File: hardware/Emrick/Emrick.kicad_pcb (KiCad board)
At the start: 4 copper layers, 44.4 x 59.2 mm, 90 parts, among them J1 LED_STRIP_CONNECTOR, J3 Conn_02x05_Odd_Even, J4 BATT_CONN, P1 USB_C_Plug_USB2.0, Q1 Q_NMOS_GSD, Q2 Q_NMOS_GSD, Q3 Q_NMOS_GSD, SW1 SW_SPST, SW2 SW_Push_LED, U1 74HCT541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

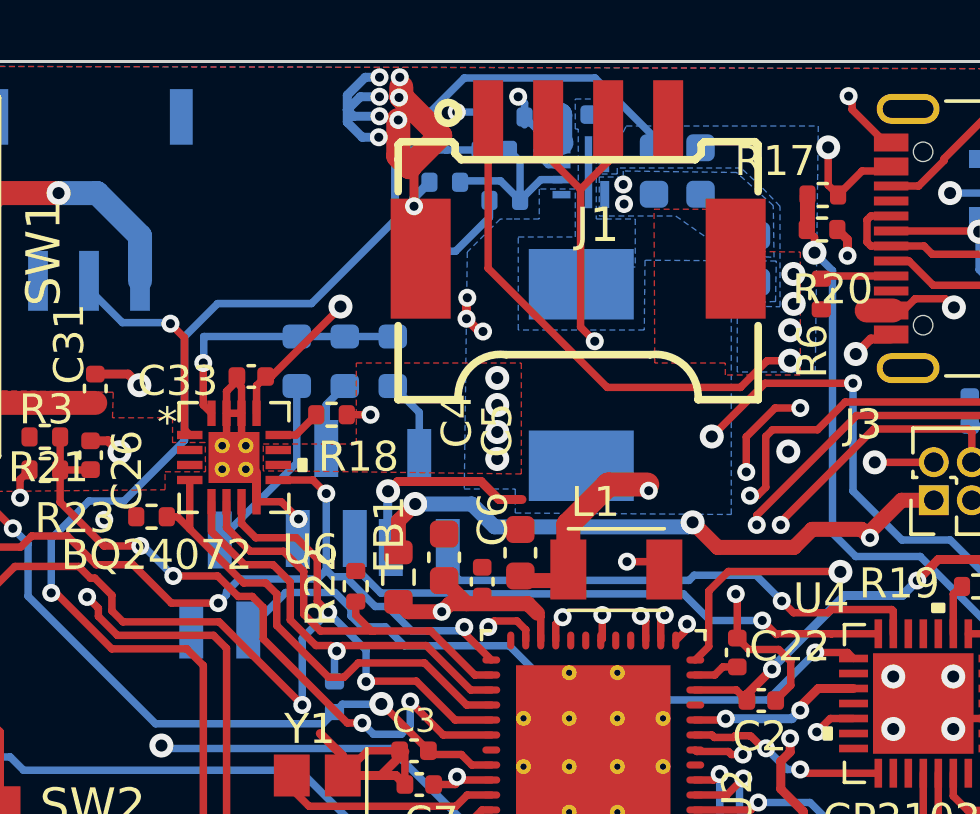
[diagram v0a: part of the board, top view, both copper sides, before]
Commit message: Moved inductor
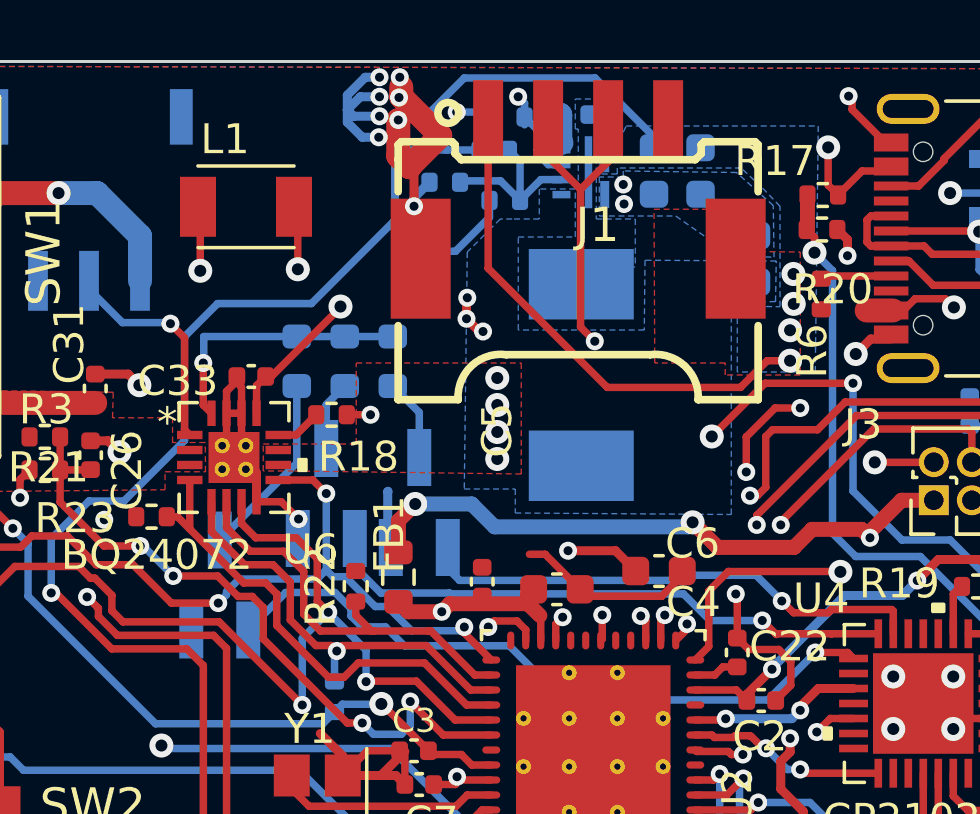
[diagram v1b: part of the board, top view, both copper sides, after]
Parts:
- moved L1 17.3 mm to (93.6, 21.8)
- moved C6 4.66 mm to (107.4, 33.9), turned to 0 degrees
- moved C4 3.91 mm to (104.0, 34.5), turned to 0 degrees
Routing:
- net DCDC_SW: track 5.14 -> 20.1 mm
- net VDDR: track 26.3 -> 36.9 mm, vias 3 -> 4
- net GND: track 89.3 -> 90.4 mm, vias 59 -> 57
- net VDDS: track 151.2 -> 150.2 mm

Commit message: Moved inductor away from connector
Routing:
- net GND: vias 57 -> 56
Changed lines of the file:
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@@
   (via (at 111 44.05) (size 0.6) (drill 0.3) (layers "F.Cu" "B.Cu") (net 2))
   (via (at 119.075 60.15) (size 0.6) (drill 0.3) (layers "F.Cu" "B.Cu") (free) (net 2))
-  (via (at 102.925 60) (size 0.6) (drill 0.3) (layers "F.Cu" "B.Cu") (free) (net 2))
   (via (at 105.9 54.6) (size 0.6) (drill 0.3) (layers "F.Cu" "B.Cu") (free) (net 2))
   (via (at 98.075 18.125) (size 0.6) (drill 0.3) (layers "F.Cu" "B.Cu") (free) (net 2))

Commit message: Started connecting pins for rev 6.0
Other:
- board text added: "Emrick Rev 6.0 1/25/2024"
- board text added: "Rev 6.0 Board #"
- board text removed: "Emrick Rev 5.2 11/5/2023"
- board text removed: "Rev 5.2 Board #"
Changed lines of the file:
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@@
   (gr_line (start 83.1 38.3) (end 122.4 38.4)
     (stroke (width 0.1) (type default)) (layer "B.Fab"))
-  (gr_text "Emrick Rev 5.2 11/5/2023\n" (at 100.9 44.575) (layer "B.SilkS")
+  (gr_text "Emrick Rev 6.0 1/25/2024\n" (at 100.9 44.575) (layer "B.SilkS")
     (effects (font (size 1.5 1.5) (thickness 0.3)) (justify mirror))
   )
@@
     (effects (font (size 1 1) (thickness 0.15)))
   )
-  (gr_text "Rev 5.2 Board #" (at 80.45 67.35) (layer "F.SilkS")
+  (gr_text "Rev 6.0 Board #" (at 80.45 67.35) (layer "F.SilkS")
     (effects (font (size 3 3) (thickness 0.3)) (justify left bottom))
   )

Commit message: Added 1312 to pcb layout
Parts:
- U2: value CC1310 -> CC1312R1F3RGZ; footprint cc1310:CC1310F128RGZR -> Package_DFN_QFN:VQFN-48-1EP_7x7mm_P0.5mm_EP5.15x5.15mm
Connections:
- C22 pad 1: Net-(U2-DCOUPL) -> GND
- C22 pad 2: GND -> Net-(U2-DCOUPL)
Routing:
- net GND: track 90.4 -> 91.9 mm
- net Net-(U2-DCOUPL): track 1.51 -> 0.00 mm

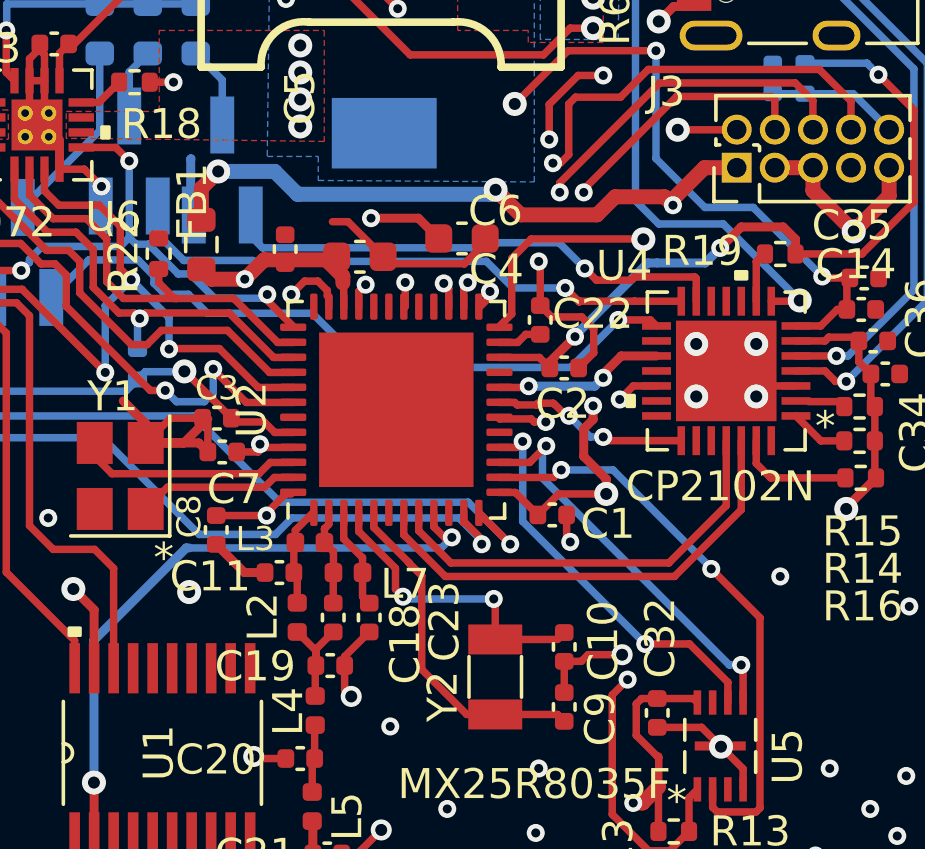
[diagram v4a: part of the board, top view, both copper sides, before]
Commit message: Fixed pin errors on pcb for cc1312
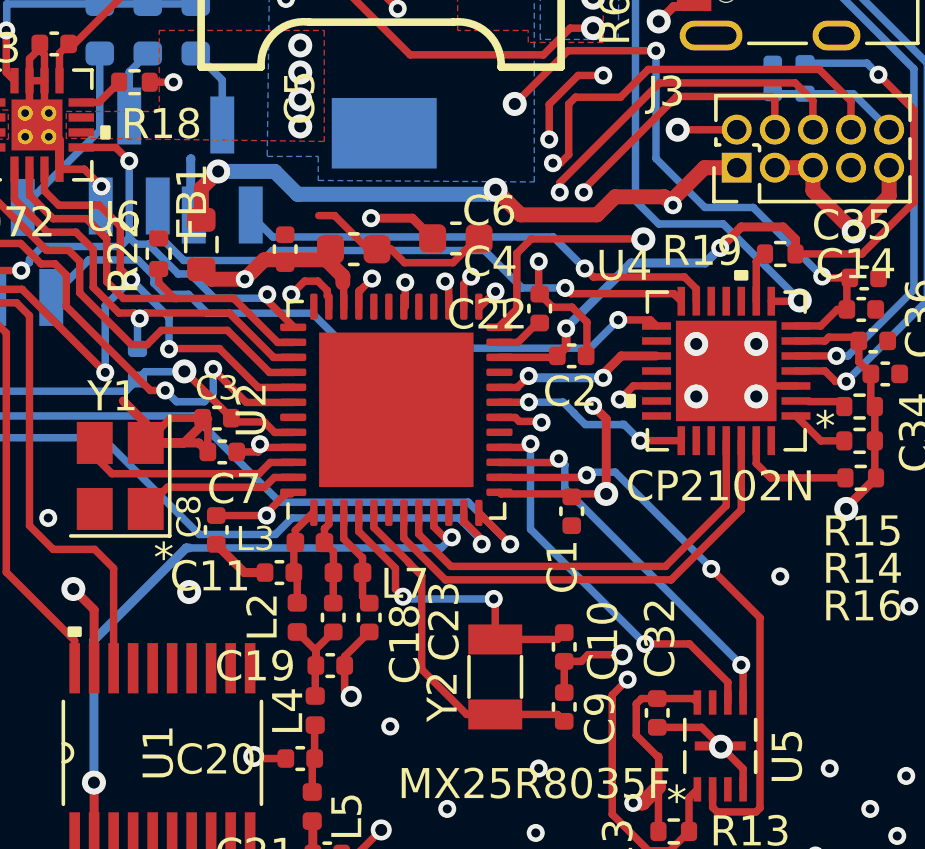
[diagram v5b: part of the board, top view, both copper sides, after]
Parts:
- moved C1 0.66 mm to (111.0, 43.0), turned to -90 degrees
- moved C2 0.47 mm to (111.0, 37.8)
- moved C22 0.38 mm to (110.0, 36.3), turned to -90 degrees
- moved C4 0.33 mm to (103.8, 34.3)
- moved C6 0.20 mm to (107.2, 33.9)
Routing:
- net GND: track 91.9 -> 89.1 mm, vias 56 -> 55
- net Net-(U2-DCOUPL): track 0.00 -> 1.65 mm
- net CHREN: track 17.1 -> 16.3 mm
- net DIO9_Flash_MOSI: track 13.4 -> 12.7 mm
- net VDDS: track 150.1 -> 149.5 mm
- net CHR0: track 23.1 -> 22.5 mm

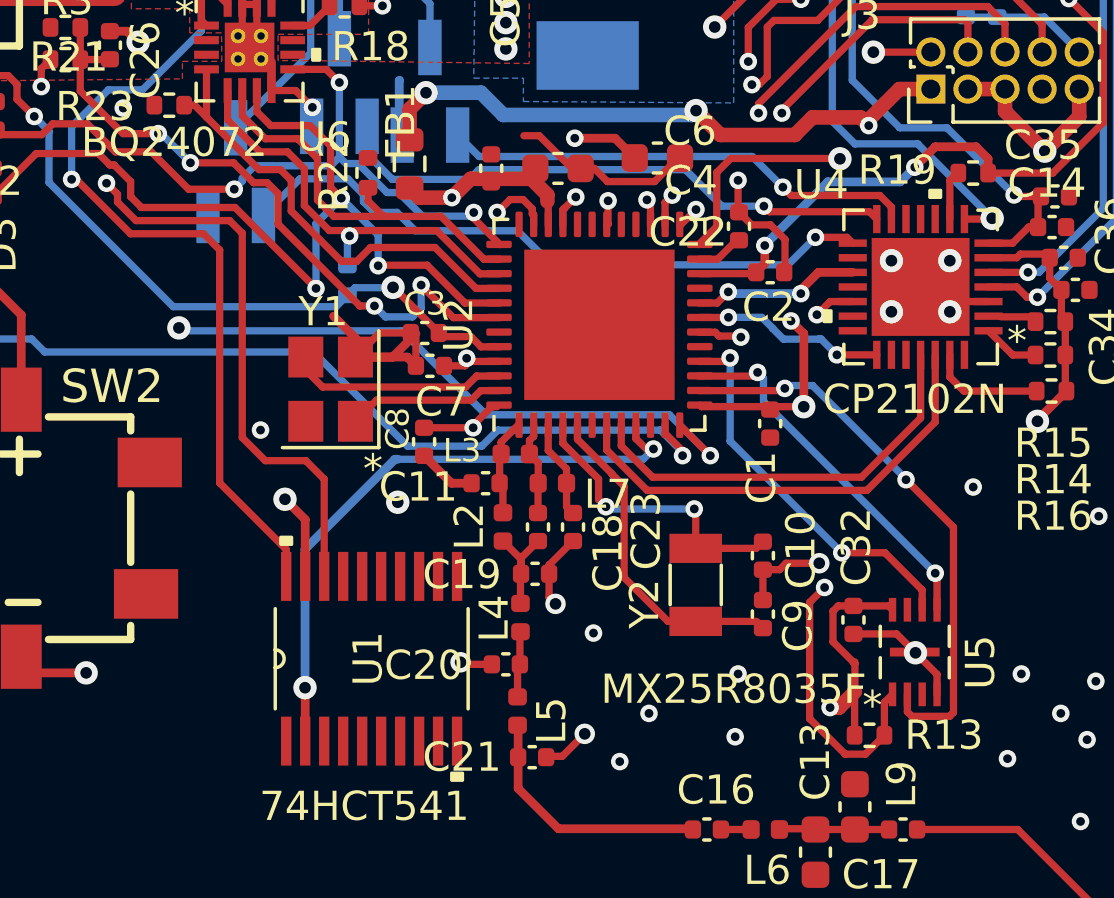
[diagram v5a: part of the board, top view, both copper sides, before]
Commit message: Connected cc1312 in pcb
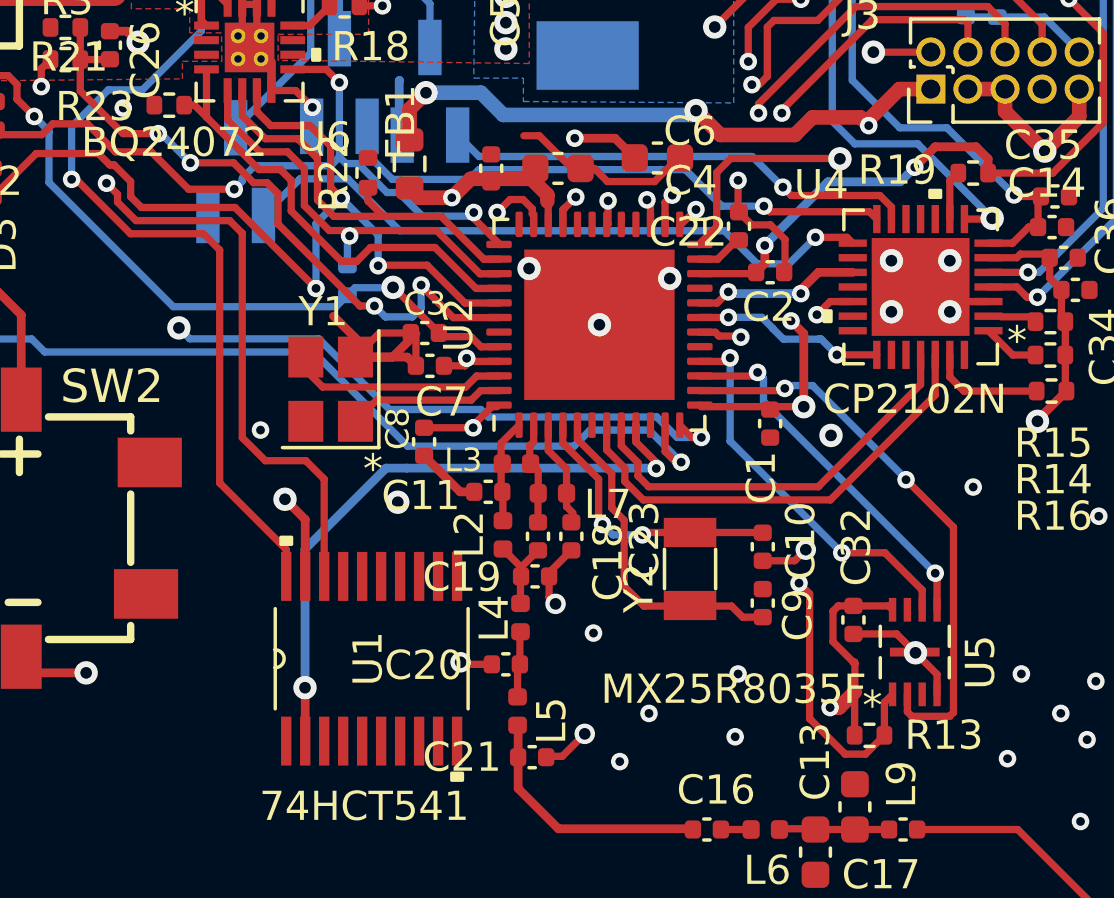
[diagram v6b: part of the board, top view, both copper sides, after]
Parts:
- moved Y2 0.58 mm to (108.3, 48.0)
- moved C9 0.38 mm to (110.8, 49.2)
- moved L7 0.35 mm to (103.6, 45.4)
- moved L3 0.33 mm to (102.4, 44.4)
- moved C23 0.32 mm to (104.2, 46.9)
- moved C18 0.32 mm to (103.1, 46.9)
- moved C11 0.31 mm to (101.4, 45.4)
- moved C10 0.31 mm to (110.8, 47.2)
- moved L2 0.27 mm to (101.9, 46.8)
- moved C19 0.09 mm to (103.0, 48.3)
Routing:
- net GND: track 89.1 -> 87.5 mm, vias 55 -> 59
- net PWR_LED: track 37.1 -> 35.9 mm
- net LED_DATA_3V: track 21.2 -> 22.0 mm
- net Net-(U2-X32K_Q1): track 10.3 -> 9.67 mm
- net Net-(C18-Pad2): track 3.76 -> 3.17 mm
